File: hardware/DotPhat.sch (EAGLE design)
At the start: 58 parts, among them CN1 1X4-BIG, IC1 CAT24M010TS, IC3 SI1145, J3 USB-MICROB, Q1 BSH103, U1 ATMEGA328P-MU-QFN32, U2 TMP102, U3 ATSHA204-TSU, X2 MC-RTC-RV-4162-C7-I2C, X3 S4B-ZR

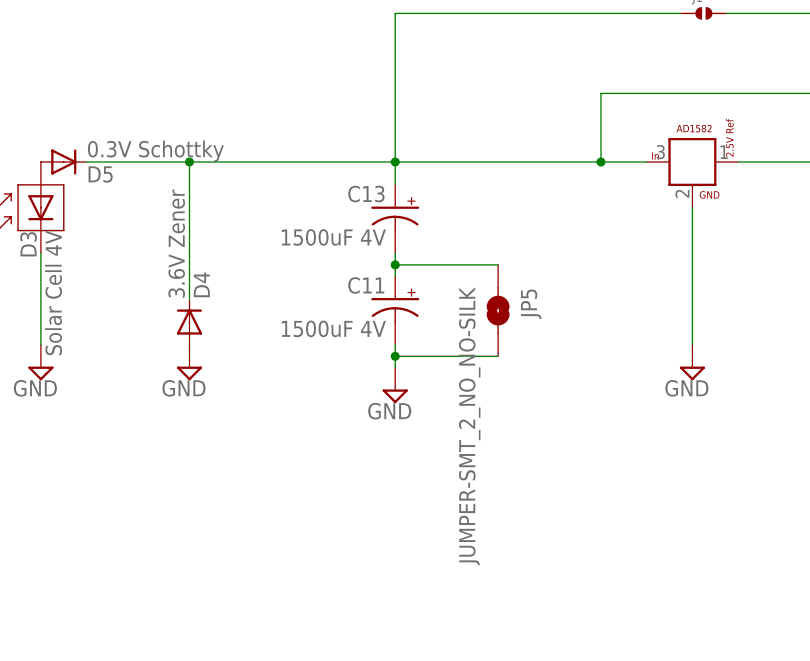
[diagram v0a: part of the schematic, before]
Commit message: Revert "Move caps from parallel to series"
This reverts commit e29ebe1b9370ccceb9c5010c93145ac8bd52b422.
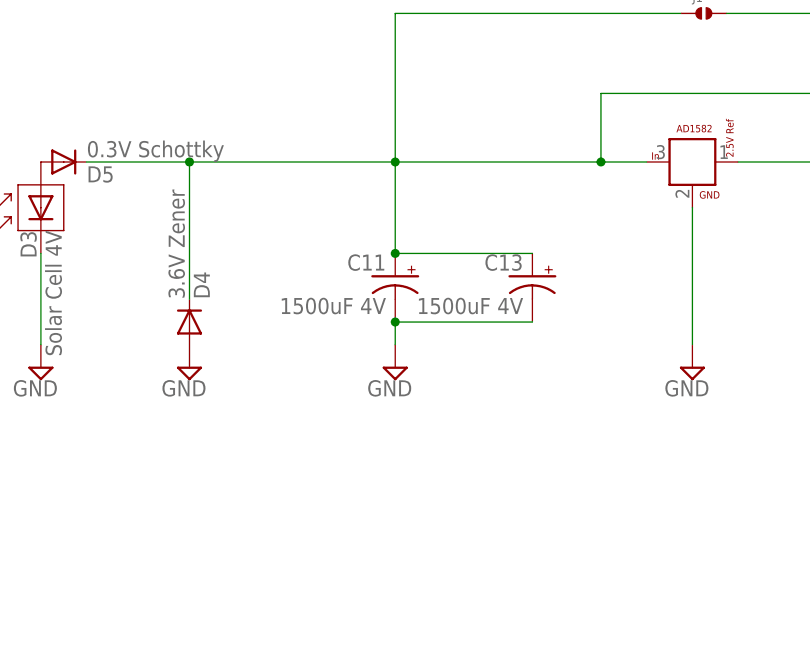
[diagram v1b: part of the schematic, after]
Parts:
- removed JP5: JUMPER-SMT_2_NO_NO-SILK, SparkFun-Jumpers:JUMPER-SMT_2_NO_NO-SILK
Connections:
- removed net N$25: C11.+, C13.-, JP5.1
- net CAPS_VCC: now also C11.+
- net GND: now also C13.-; no longer JP5.2
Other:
- moved on the sheet: C11, C13
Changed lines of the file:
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@@
 <part name="TP1" library="SparkFun" deviceset="TEST-POINT" device="3"/>
 <part name="J1" library="solderjumper" deviceset="SOLDERJUMPER.2" device=".MED"/>
-<part name="JP5" library="SparkFun-Jumpers" deviceset="JUMPER-SMT_2_NO" device="_NO-SILK"/>
 </parts>
 <sheets>
@@
 <instance part="D4" gate="G$1" x="8.89" y="-227.33" rot="MR90"/>
 <instance part="SUPPLY33" gate="GND" x="-7.62" y="-232.41" rot="MR0"/>
-<instance part="C11" gate="G$1" x="31.75" y="-224.79" rot="MR0"/>
-<instance part="SUPPLY35" gate="GND" x="31.75" y="-234.95" rot="MR0"/>
-<instance part="C13" gate="G$1" x="31.75" y="-214.63" rot="MR0"/>
+<instance part="C11" gate="G$1" x="31.75" y="-222.25" rot="MR0"/>
+<instance part="SUPPLY35" gate="GND" x="31.75" y="-232.41" rot="MR0"/>
+<instance part="C13" gate="G$1" x="46.99" y="-222.25" rot="MR0"/>
 <instance part="SUPPLY34" gate="GND" x="8.89" y="-232.41" rot="MR0"/>
 <instance part="+3V22" gate="G$1" x="113.03" y="-187.96" rot="MR0"/>
@@
 <instance part="TP1" gate="G$1" x="-50.8" y="68.58" rot="R180"/>
 <instance part="J1" gate="G$1" x="66.04" y="-193.04"/>
-<instance part="JP5" gate="G$1" x="43.18" y="-226.06" rot="R270"/>
 </instances>
 <busses>
@@
 </segment>
 <segment>
+<pinref part="C11" gate="G$1" pin="-"/>
+<pinref part="SUPPLY35" gate="GND" pin="GND"/>
+<wire x1="31.75" y1="-227.33" x2="31.75" y2="-229.87" width="0.1524" layer="91"/>
+<junction x="31.75" y="-227.33"/>
+<pinref part="C13" gate="G$1" pin="-"/>
+<wire x1="31.75" y1="-227.33" x2="46.99" y2="-227.33" width="0.1524" layer="91"/>
+</segment>
+<segment>
 <pinref part="D4" gate="G$1" pin="A"/>
 <pinref part="SUPPLY34" gate="GND" pin="GND"/>
@@
 <pinref part="IC3" gate="G$1" pin="GND"/>
 <pinref part="SUPPLY37" gate="GND" pin="GND"/>
-</segment>
-<segment>
-<pinref part="SUPPLY35" gate="GND" pin="GND"/>
-<pinref part="C11" gate="G$1" pin="-"/>
-<wire x1="31.75" y1="-232.41" x2="31.75" y2="-231.14" width="0.1524" layer="91"/>
-<pinref part="JP5" gate="G$1" pin="2"/>
-<wire x1="31.75" y1="-231.14" x2="31.75" y2="-229.87" width="0.1524" layer="91"/>
-<wire x1="43.18" y1="-231.14" x2="31.75" y2="-231.14" width="0.1524" layer="91"/>
-<junction x="31.75" y="-231.14"/>
 </segment>
 </net>
@@
 <net name="CAPS_VCC" class="0">
 <segment>
+<pinref part="C13" gate="G$1" pin="+"/>
+<pinref part="C11" gate="G$1" pin="+"/>
+<wire x1="46.99" y1="-219.71" x2="31.75" y2="-219.71" width="0.1524" layer="91"/>
+<junction x="31.75" y="-219.71"/>
 <pinref part="U$4" gate="G$1" pin="P$3"/>
 <wire x1="59.69" y1="-209.55" x2="54.61" y2="-209.55" width="0.1524" layer="91"/>
 <wire x1="54.61" y1="-209.55" x2="31.75" y2="-209.55" width="0.1524" layer="91"/>
+<wire x1="31.75" y1="-209.55" x2="31.75" y2="-219.71" width="0.1524" layer="91"/>
 <pinref part="D5" gate="G$1" pin="C"/>
 <wire x1="-2.54" y1="-209.55" x2="8.89" y2="-209.55" width="0.1524" layer="91"/>
@@
 <wire x1="63.5" y1="-193.04" x2="31.75" y2="-193.04" width="0.1524" layer="91"/>
 <wire x1="31.75" y1="-193.04" x2="31.75" y2="-209.55" width="0.1524" layer="91"/>
-<pinref part="C13" gate="G$1" pin="+"/>
-<wire x1="31.75" y1="-209.55" x2="31.75" y2="-212.09" width="0.1524" layer="91"/>
 </segment>
 </net>
@@
 </segment>
 </net>
-<net name="N$25" class="0">
-<segment>
-<pinref part="C11" gate="G$1" pin="+"/>
-<pinref part="C13" gate="G$1" pin="-"/>
-<wire x1="31.75" y1="-222.25" x2="31.75" y2="-220.98" width="0.1524" layer="91"/>
-<pinref part="JP5" gate="G$1" pin="1"/>
-<wire x1="31.75" y1="-220.98" x2="31.75" y2="-219.71" width="0.1524" layer="91"/>
-<wire x1="43.18" y1="-220.98" x2="31.75" y2="-220.98" width="0.1524" layer="91"/>
-<junction x="31.75" y="-220.98"/>
-</segment>
-</net>

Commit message: Move caps from parallel to series
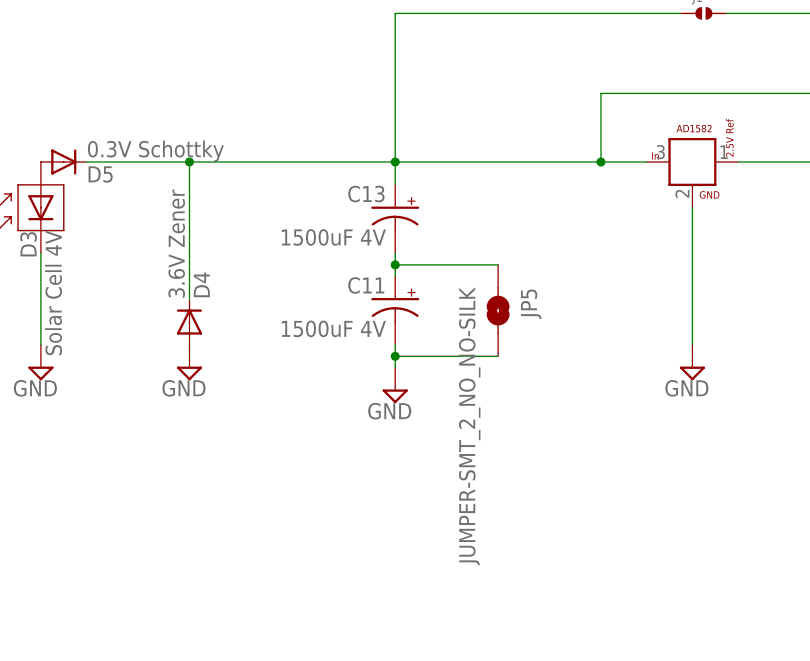
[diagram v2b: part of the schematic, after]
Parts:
- added JP5: JUMPER-SMT_2_NO_NO-SILK, SparkFun-Jumpers:JUMPER-SMT_2_NO_NO-SILK
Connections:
- new net N$25: C11.+, C13.-, JP5.1
- net CAPS_VCC: no longer C11.+
- net GND: now also JP5.2; no longer C13.-
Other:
- moved on the sheet: C11, C13
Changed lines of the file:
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@@
 <part name="TP1" library="SparkFun" deviceset="TEST-POINT" device="3"/>
 <part name="J1" library="solderjumper" deviceset="SOLDERJUMPER.2" device=".MED"/>
+<part name="JP5" library="SparkFun-Jumpers" deviceset="JUMPER-SMT_2_NO" device="_NO-SILK"/>
 </parts>
 <sheets>
@@
 <instance part="D4" gate="G$1" x="8.89" y="-227.33" rot="MR90"/>
 <instance part="SUPPLY33" gate="GND" x="-7.62" y="-232.41" rot="MR0"/>
-<instance part="C11" gate="G$1" x="31.75" y="-222.25" rot="MR0"/>
-<instance part="SUPPLY35" gate="GND" x="31.75" y="-232.41" rot="MR0"/>
-<instance part="C13" gate="G$1" x="46.99" y="-222.25" rot="MR0"/>
+<instance part="C11" gate="G$1" x="31.75" y="-224.79" rot="MR0"/>
+<instance part="SUPPLY35" gate="GND" x="31.75" y="-234.95" rot="MR0"/>
+<instance part="C13" gate="G$1" x="31.75" y="-214.63" rot="MR0"/>
 <instance part="SUPPLY34" gate="GND" x="8.89" y="-232.41" rot="MR0"/>
 <instance part="+3V22" gate="G$1" x="113.03" y="-187.96" rot="MR0"/>
@@
 <instance part="TP1" gate="G$1" x="-50.8" y="68.58" rot="R180"/>
 <instance part="J1" gate="G$1" x="66.04" y="-193.04"/>
+<instance part="JP5" gate="G$1" x="43.18" y="-226.06" rot="R270"/>
 </instances>
 <busses>
@@
 </segment>
 <segment>
-<pinref part="C11" gate="G$1" pin="-"/>
-<pinref part="SUPPLY35" gate="GND" pin="GND"/>
-<wire x1="31.75" y1="-227.33" x2="31.75" y2="-229.87" width="0.1524" layer="91"/>
-<junction x="31.75" y="-227.33"/>
-<pinref part="C13" gate="G$1" pin="-"/>
-<wire x1="31.75" y1="-227.33" x2="46.99" y2="-227.33" width="0.1524" layer="91"/>
-</segment>
-<segment>
 <pinref part="D4" gate="G$1" pin="A"/>
 <pinref part="SUPPLY34" gate="GND" pin="GND"/>
@@
 <pinref part="IC3" gate="G$1" pin="GND"/>
 <pinref part="SUPPLY37" gate="GND" pin="GND"/>
+</segment>
+<segment>
+<pinref part="SUPPLY35" gate="GND" pin="GND"/>
+<pinref part="C11" gate="G$1" pin="-"/>
+<wire x1="31.75" y1="-232.41" x2="31.75" y2="-231.14" width="0.1524" layer="91"/>
+<pinref part="JP5" gate="G$1" pin="2"/>
+<wire x1="31.75" y1="-231.14" x2="31.75" y2="-229.87" width="0.1524" layer="91"/>
+<wire x1="43.18" y1="-231.14" x2="31.75" y2="-231.14" width="0.1524" layer="91"/>
+<junction x="31.75" y="-231.14"/>
 </segment>
 </net>
@@
 <net name="CAPS_VCC" class="0">
 <segment>
-<pinref part="C13" gate="G$1" pin="+"/>
-<pinref part="C11" gate="G$1" pin="+"/>
-<wire x1="46.99" y1="-219.71" x2="31.75" y2="-219.71" width="0.1524" layer="91"/>
-<junction x="31.75" y="-219.71"/>
 <pinref part="U$4" gate="G$1" pin="P$3"/>
 <wire x1="59.69" y1="-209.55" x2="54.61" y2="-209.55" width="0.1524" layer="91"/>
 <wire x1="54.61" y1="-209.55" x2="31.75" y2="-209.55" width="0.1524" layer="91"/>
-<wire x1="31.75" y1="-209.55" x2="31.75" y2="-219.71" width="0.1524" layer="91"/>
 <pinref part="D5" gate="G$1" pin="C"/>
 <wire x1="-2.54" y1="-209.55" x2="8.89" y2="-209.55" width="0.1524" layer="91"/>
@@
 <wire x1="63.5" y1="-193.04" x2="31.75" y2="-193.04" width="0.1524" layer="91"/>
 <wire x1="31.75" y1="-193.04" x2="31.75" y2="-209.55" width="0.1524" layer="91"/>
+<pinref part="C13" gate="G$1" pin="+"/>
+<wire x1="31.75" y1="-209.55" x2="31.75" y2="-212.09" width="0.1524" layer="91"/>
 </segment>
 </net>
@@
 </segment>
 </net>
+<net name="N$25" class="0">
+<segment>
+<pinref part="C11" gate="G$1" pin="+"/>
+<pinref part="C13" gate="G$1" pin="-"/>
+<wire x1="31.75" y1="-222.25" x2="31.75" y2="-220.98" width="0.1524" layer="91"/>
+<pinref part="JP5" gate="G$1" pin="1"/>
+<wire x1="31.75" y1="-220.98" x2="31.75" y2="-219.71" width="0.1524" layer="91"/>
+<wire x1="43.18" y1="-220.98" x2="31.75" y2="-220.98" width="0.1524" layer="91"/>
+<junction x="31.75" y="-220.98"/>
+</segment>
+</net>
